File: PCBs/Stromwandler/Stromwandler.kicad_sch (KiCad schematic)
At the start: 10 parts, among them IC1 HO10-P_SP33, J1 Conn_02x05_Odd_Even, J4 2X

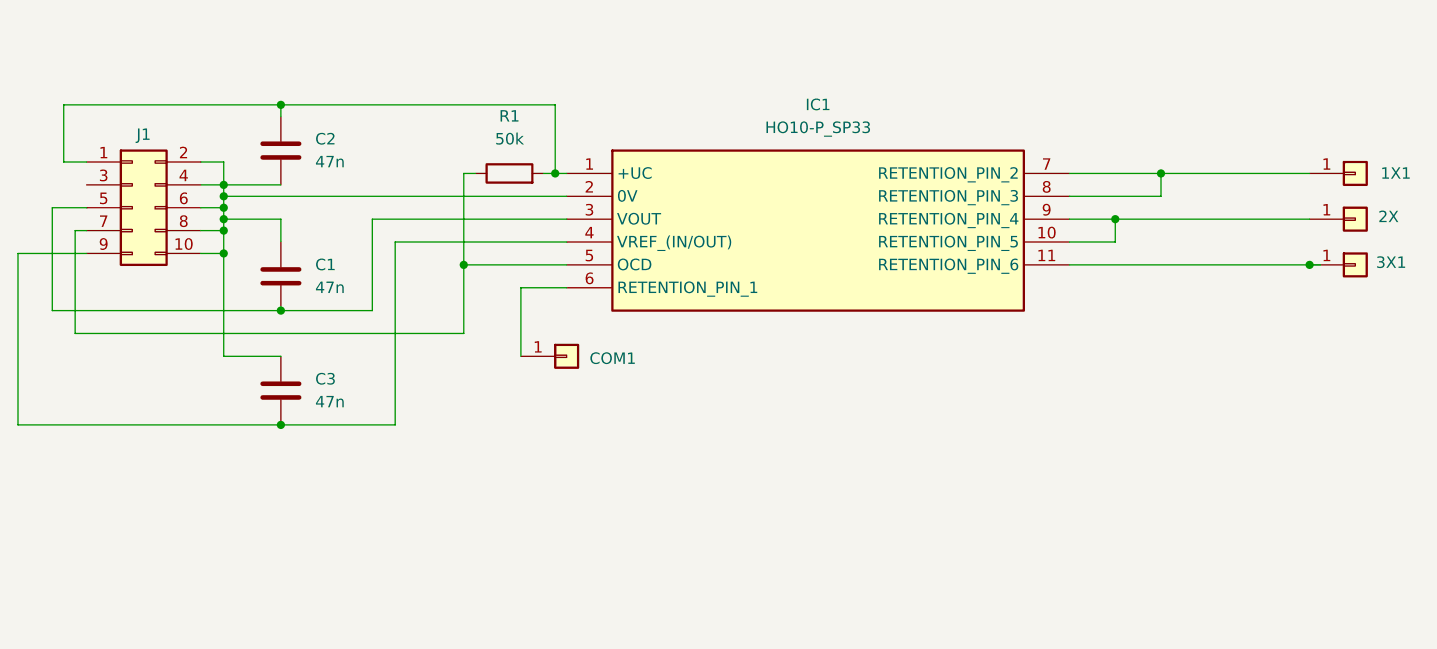
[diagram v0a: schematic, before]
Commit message: Zusammenfuehrung
PCB und SCH Update zu 7-polig. Mehr übersichtlichkeit und Update Footprints Connectoren
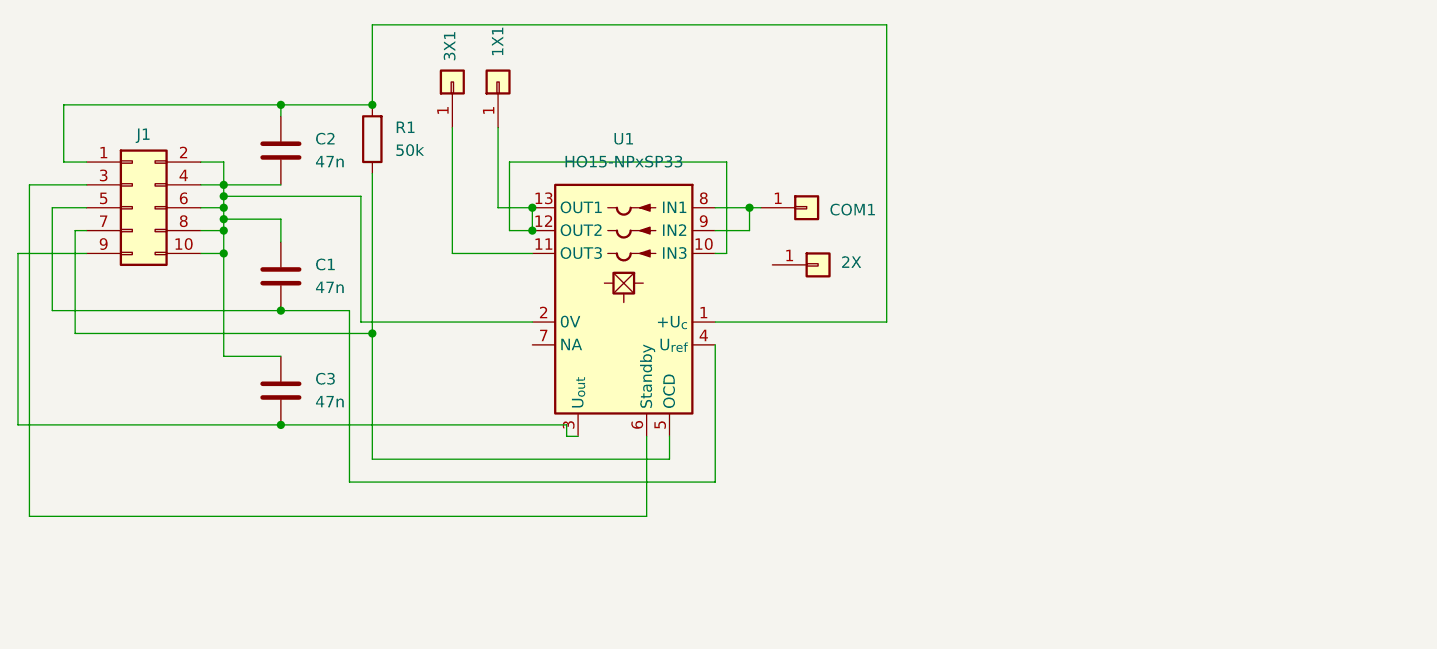
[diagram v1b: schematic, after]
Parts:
- removed IC1: HO10-P_SP33, HO10_P_SP33:HO10PSP33, symbol HO10-P_SP33:HO10-P_SP33
- added U1: HO15-NPxSP33, Sensor_Current:LEM_HO8-NP, symbol Sensor_Current:HO15-NPxSP33
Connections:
- net at C2.1, J1.1 (Pin_1), R1.2: now also U1.1 (+U_{c})
- net at C1.1, C2.2, C3.1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: now also U1.2 (0V)
- net at J1.3 (Pin_3): now also U1.6 (Standby)
- net at C1.2, J1.5 (Pin_5): now also U1.4 (U_{ref})
- net at J1.7 (Pin_7), R1.1: now also U1.5 (OCD)
- net at C3.2, J1.9 (Pin_9): now also U1.3 (U_{out})
- net at COM1.1 (Pin_1): now also U1.8 (IN1), U1.9 (IN2)
- net at 3X1.1 (Pin_1): now also U1.11 (OUT3)
- net at 1X1.1 (Pin_1): now also U1.10 (IN3), U1.12 (OUT2), U1.13 (OUT1)
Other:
- moved on the sheet: 1X1, 3X1, COM1, R1

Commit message: Korrekturen: Anordnung 4mm-Pins Tausch Stecker Pin 5 7 (Uref, OCD) GND Vias (noch mehr  notwendig / Anordnung pruefen)
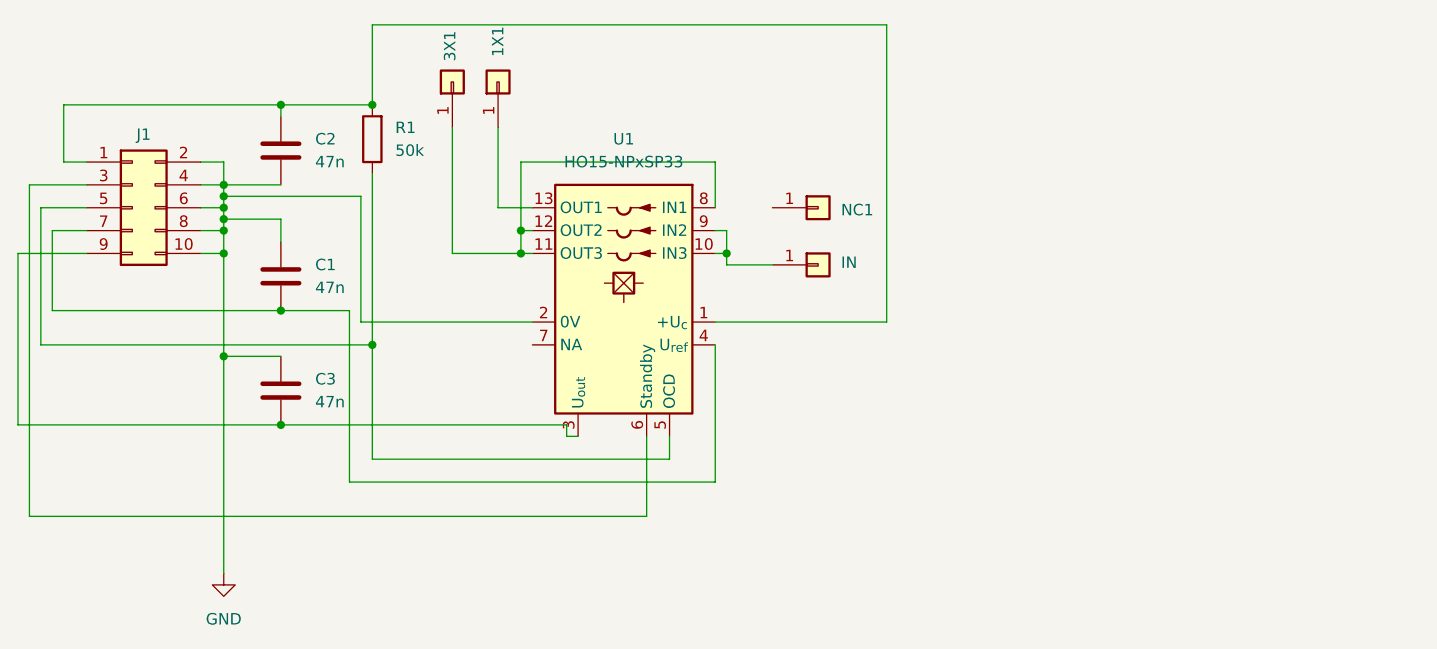
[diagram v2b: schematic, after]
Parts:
- J4: value 2X -> IN
- renumbered COM1 to NC1
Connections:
- net GND: now reaches C1.1, C2.2, C3.1, J1.10 (Pin_10), J1.2 (Pin_2), J1.4 (Pin_4), J1.6 (Pin_6), J1.8 (Pin_8), U1.2 (0V)
- net at C1.2, U1.4 (U_{ref}): now also J1.7 (Pin_7); no longer J1.5 (Pin_5)
- net at R1.1, U1.5 (OCD): now also J1.5 (Pin_5); no longer J1.7 (Pin_7)
- net at 1X1.1 (Pin_1), U1.13 (OUT1): no longer U1.10 (IN3), U1.12 (OUT2)
- net at J4.1 (Pin_1): now also U1.10 (IN3), U1.9 (IN2)
- net at 3X1.1 (Pin_1), U1.11 (OUT3): now also U1.12 (OUT2), U1.8 (IN1)
- now unconnected: NC1.1 (Pin_1)
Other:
- moved on the sheet: NC1
